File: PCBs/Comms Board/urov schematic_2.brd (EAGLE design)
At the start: 100 x 80 mm, 24 parts

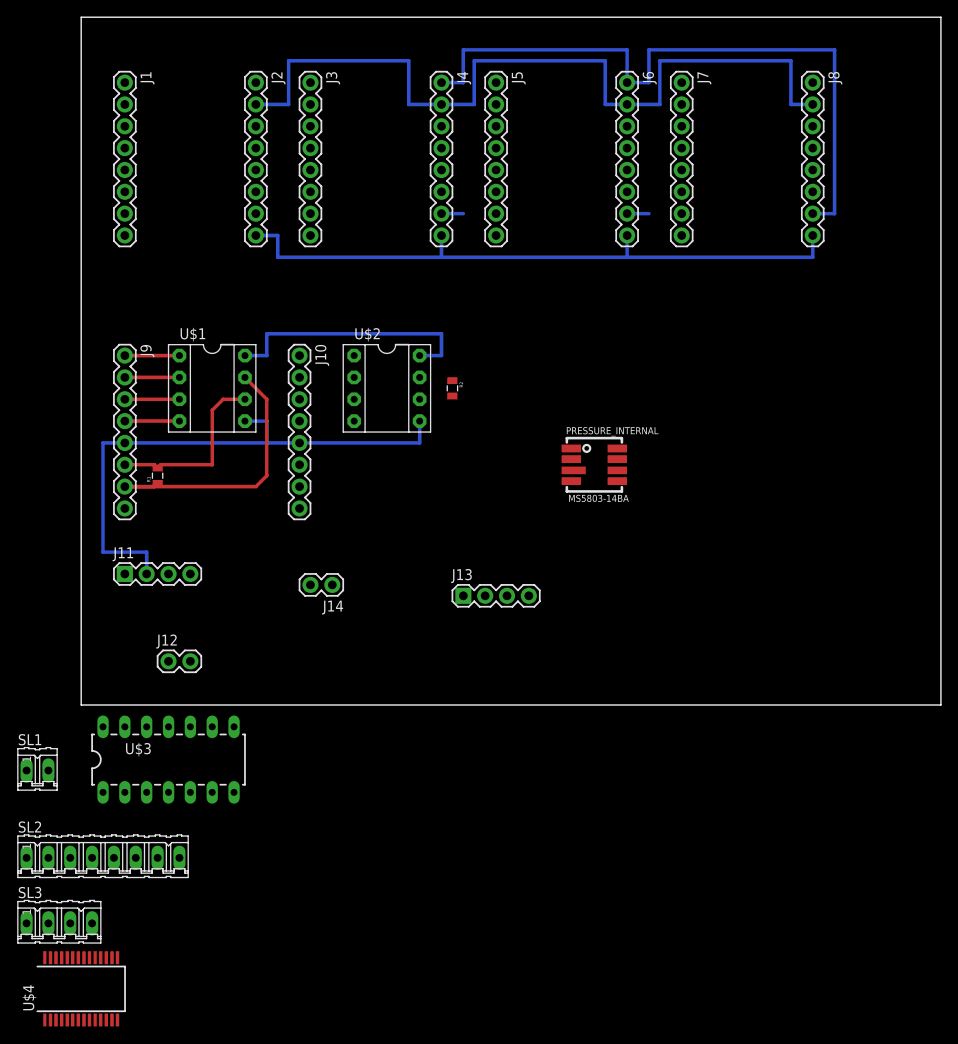
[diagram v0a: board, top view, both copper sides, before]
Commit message: updated board
rearranged board configuration, added wago screw clamps
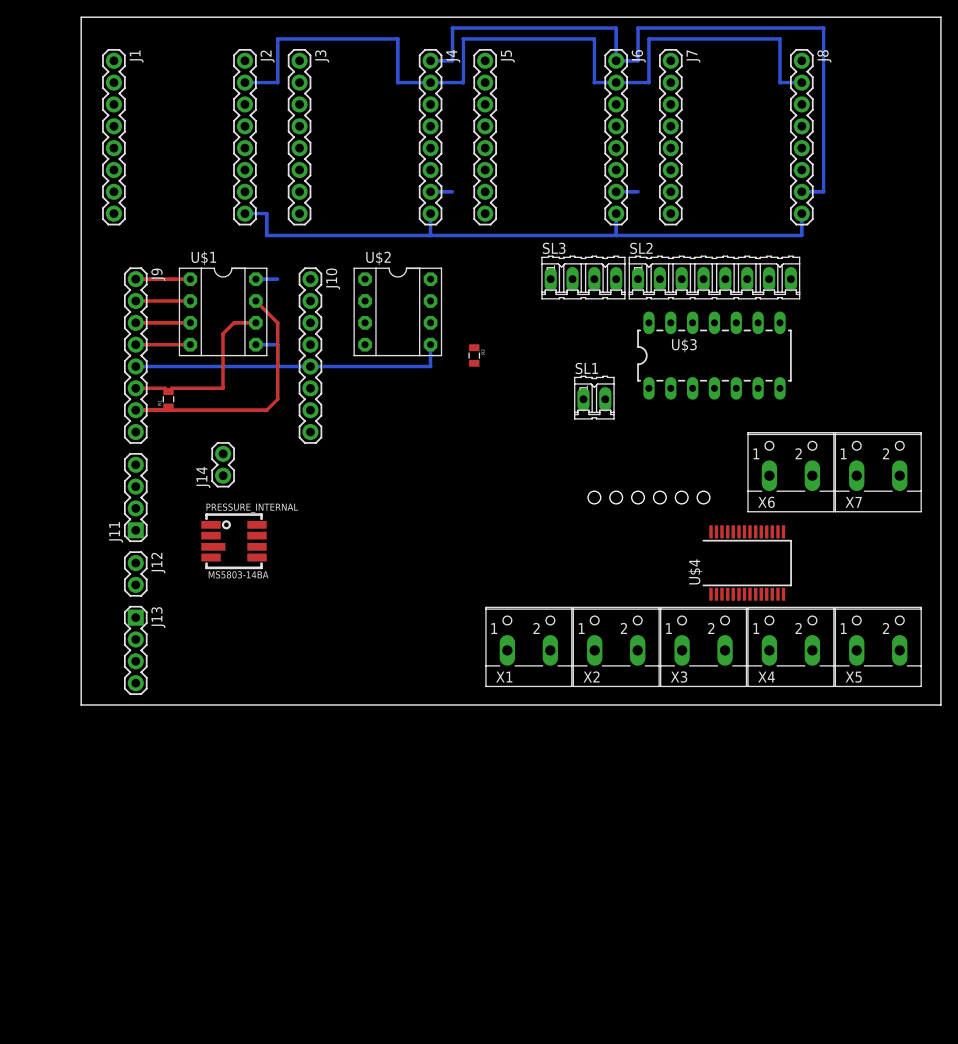
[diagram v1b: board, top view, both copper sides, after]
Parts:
- added J16: (no value), SparkFun-Connectors:1X06_HOLES_ONLY
- added X1, X2, X3, X4, X5, X6, X7: (no value), con-wago-500:W237-102
- moved SL2 97.9 mm to (73.7, 49.5)
- moved SL3 96.6 mm to (58.4, 49.5)
- moved U$4 92.0 mm to (77.5, 16.5)
- moved U$3 79.0 mm to (74.9, 40.6)
- moved SL1 77.8 mm to (59.7, 35.6)
- moved PRESSURE_INTERNAL 42.8 mm to (17.8, 19.1)
- moved J13 38.2 mm to (6.35, 10.2), turned to 270 degrees
- moved J14 18.0 mm to (16.5, 26.7), turned to 90 degrees
- moved J12 12.0 mm to (6.35, 16.5), turned to 270 degrees
- moved J10 8.98 mm to (26.7, 49.5)
- moved J9 8.98 mm to (6.35, 49.5)
- moved R1 8.98 mm to (10.2, 35.6)
- moved U$1 8.98 mm to (16.5, 45.7)
- moved U$2 8.98 mm to (36.8, 45.7)
- moved J11 5.24 mm to (6.35, 20.3), turned to 90 degrees
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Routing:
- net VDD: track 125.7 -> 97.8 mm
- net GND: track 148.6 -> 125.7 mm
